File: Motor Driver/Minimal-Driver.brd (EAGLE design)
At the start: 49.6 x 13 mm, 9 parts, among them CN1 3p-2.54, Q1 CJ2302

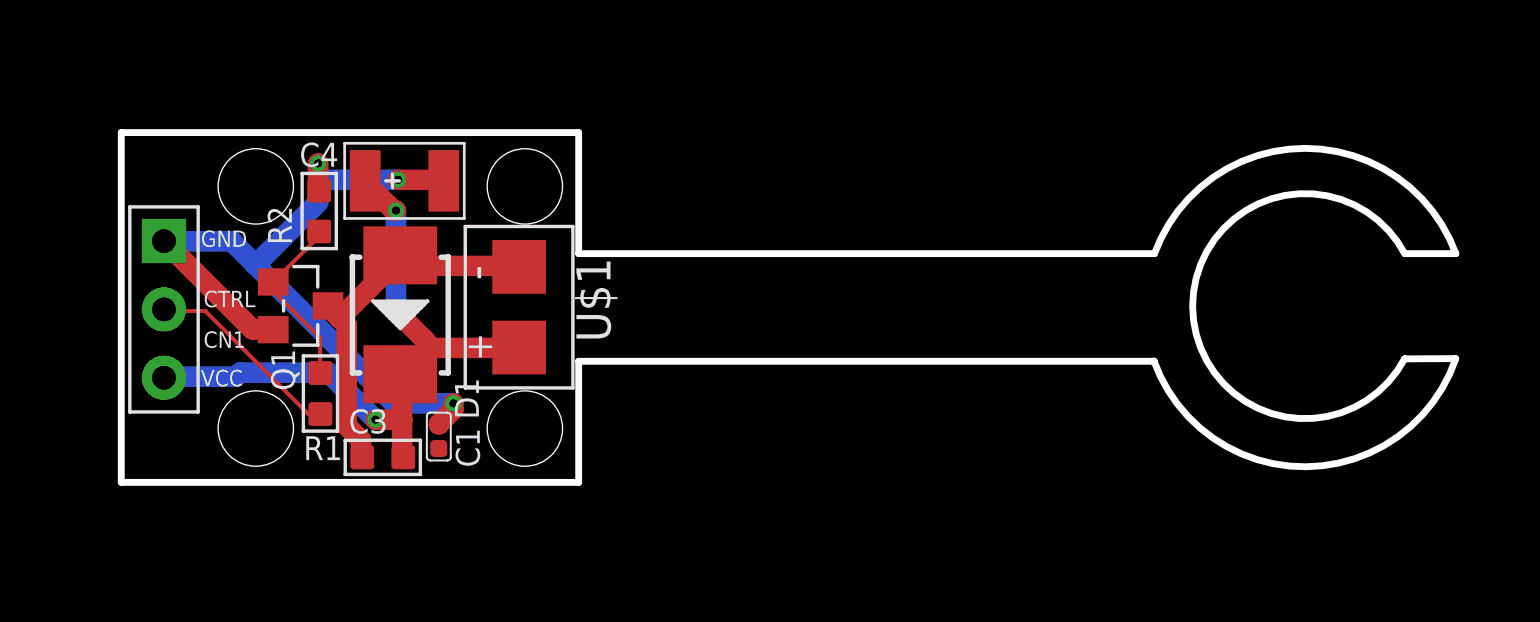
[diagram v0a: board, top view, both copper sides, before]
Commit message: New remote, new motor driver
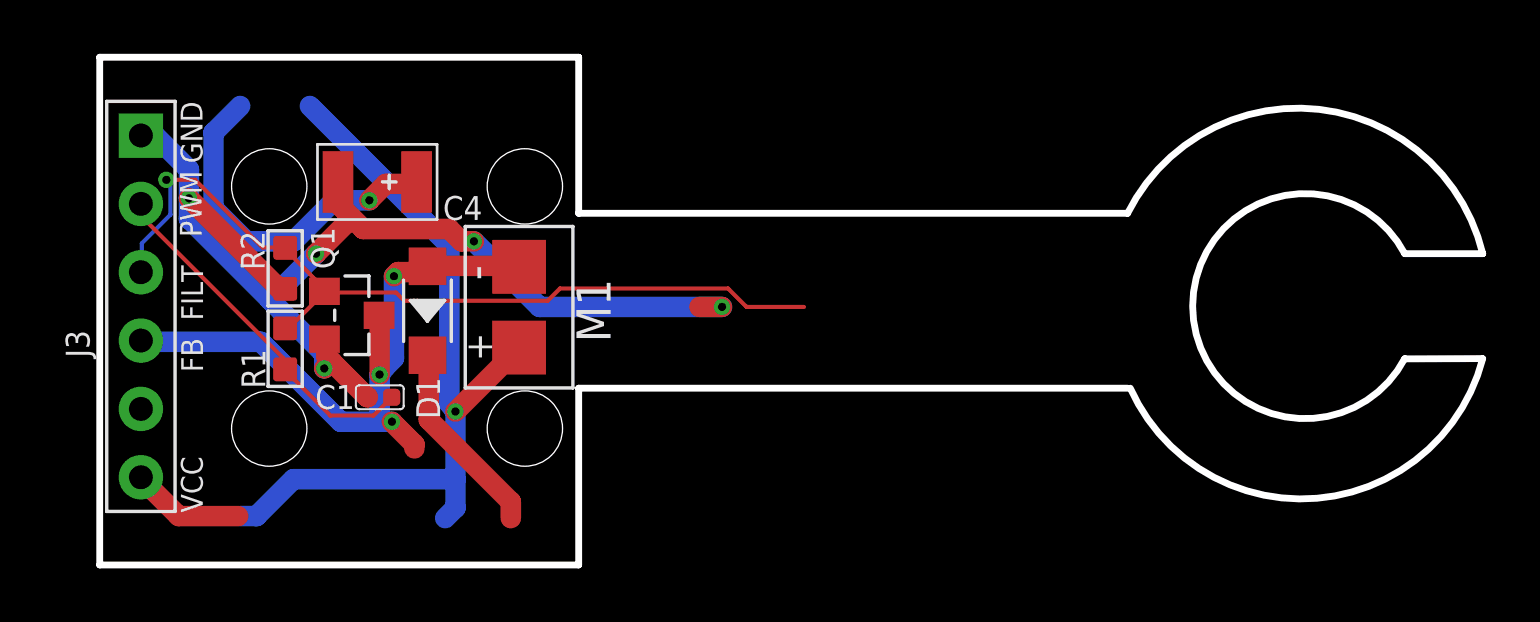
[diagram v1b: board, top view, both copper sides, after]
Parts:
- removed C3: 1uf, Seeed-Capacitor-2016:C0603
- removed CN1: 3p-2.54, Seeed-Connector -2016:H3-2.54
- added J3: 6p-2.54, Seeed-Connector -2016:H6-2.54
- D1: value 28V-5A -> 20V-500MA; device Seeed-Diode-2016:DO-214AA -> Seeed-Diode-2016:SOD-123
- moved C1 2.64 mm to (9.61, 2.66), turned to 90 degrees
- moved R2 2.48 mm to (6.09, 7.46), turned to 180 degrees
- moved R1 2.11 mm to (6.09, 4.46)
- moved Q1 1.93 mm to (8.57, 5.71)
- moved D1 1.02 mm to (11.4, 5.88)
- moved C4 1.01 mm to (9.52, 10.7), turned to 180 degrees
- renumbered U$1 to M1
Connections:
- removed net N$3: C1.2, CN1.2, R1.1
- removed net N$4: Q1.1, R1.2, R2.2
- removed net N$6: C3.1, D1.+, M1.V-, Q1.3
- new net FB: D1.+, J3.4, M1.V-, Q1.3
- new net FILT: J3.3, Q1.1, R1.2, R2.2
- new net PWM: C1.2, J3.2, R1.1
- net GND: now also J3.1; no longer CN1.1
- net VCC: now also J3.6; no longer C3.2, CN1.3
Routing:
- net FILT: track 0.00 -> 32.2 mm, vias 0 -> 1
- net VCC: track 24.9 -> 54.4 mm, vias 3 -> 2
- net FB: track 0.00 -> 24.6 mm, vias 0 -> 3
- net N$6: track 14.0 -> 0.00 mm
- net PWM: track 0.00 -> 13.4 mm
- net GND: track 30.2 -> 41.8 mm, vias 3 -> 5
- net N$3: track 7.45 -> 0.00 mm
- net N$4: track 6.71 -> 0.00 mm
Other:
- board size 49.6 x 13 mm -> 51.4 x 18.9 mm
- board text added: "FB"
- board text added: "FILT"
- board text added: "PWM"
- board text removed: "CTRL"

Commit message: cleanup
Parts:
- removed J3: 6p-2.54, Seeed-Connector -2016:H6-2.54
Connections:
- removed net FB: D1.+, J3.4, M1.V-, Q1.3
- removed net FILT: J3.3, Q1.1, R1.2, R2.2
- new net FILTERED: Q1.1, R1.2, R2.2
- new net FLYBACK: D1.+, M1.V-, Q1.3
- net GND: no longer J3.1
- net PWM: no longer J3.2
- net VCC: no longer J3.6
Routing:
- net FILT: track 32.2 -> 0.00 mm, vias 1 -> 0
- net FILTERED: track 0.00 -> 32.2 mm, vias 0 -> 1
- net FB: track 24.6 -> 0.00 mm, vias 3 -> 0
- net FLYBACK: track 0.00 -> 24.5 mm, vias 0 -> 3
- net VCC: track 54.4 -> 50.2 mm
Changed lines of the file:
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@@
 <attribute name="NAME" x="18.185" y="4.71" size="1.27" layer="21" rot="R90"/>
-</element>
-<element name="J3" library="Seeed-Connector -2016" package="H6-2.54" value="6p-2.54" x="0.73" y="6.04">
-<attribute name="MPN" value="P125-1106A1BS116A1" x="0.73" y="6.04" size="1.778" layer="27" display="off"/>
 </element>
 </elements>
@@
 <signal name="GND" class="1">
 <contactref element="C4" pad="-"/>
-<contactref element="Q1" pad="2"/>
-<contactref element="R2" pad="1"/>
-<contactref element="C1" pad="1"/>
-<contactref element="J3" pad="1"/>
 <wire x1="22.3266" y1="6.0198" x2="21.4884" y2="6.0198" width="0.762" layer="1"/>
 <wire x1="15.5448" y1="6.0198" x2="22.3266" y2="6.0198" width="0.762" layer="16"/>
@@
 <wire x1="7.8105" y1="4.0005" x2="9.144" y2="2.667" width="0.762" layer="1"/>
 <wire x1="7.62" y1="4.8006" x2="7.62" y2="4.191" width="0.762" layer="1"/>
-<wire x1="9.144" y1="2.667" x2="9.163" y2="2.6625" width="0.762" layer="1"/>
-<wire x1="7.62" y1="4.8006" x2="7.5515" y2="4.821" width="0.762" layer="1"/>
 <wire x1="5.8674" y1="6.7056" x2="6.0198" y2="6.7056" width="0.762" layer="1"/>
 <wire x1="2.5146" y1="10.0584" x2="5.8674" y2="6.7056" width="0.762" layer="1"/>
@@
 <wire x1="1.2954" y1="12.3444" x2="2.5146" y2="11.1252" width="0.762" layer="16"/>
 <wire x1="0.762" y1="12.3444" x2="1.2954" y2="12.3444" width="0.762" layer="16"/>
-<wire x1="6.0198" y1="6.7056" x2="6.0925" y2="6.693" width="0.762" layer="1"/>
-<wire x1="0.762" y1="12.3444" x2="0.73" y2="12.39" width="0.762" layer="16"/>
 <wire x1="7.5438" y1="4.2672" x2="7.5438" y2="3.7338" width="0.762" layer="16"/>
 <wire x1="2.5146" y1="9.2964" x2="5.5245" y2="6.2865" width="0.762" layer="16"/>
@@
 <via x="7.5438" y="3.7338" extent="1-16" drill="0.3048"/>
 <via x="7.239" y="8.001" extent="1-16" drill="0.3048"/>
+<contactref element="Q1" pad="2"/>
+<contactref element="R2" pad="1"/>
+<contactref element="C1" pad="1"/>
+<wire x1="6.0198" y1="6.7056" x2="6.0925" y2="6.693" width="0" layer="19" extent="1-1"/>
+<wire x1="9.163" y1="2.6625" x2="9.144" y2="2.667" width="0" layer="19" extent="1-1"/>
+<wire x1="7.5515" y1="4.821" x2="7.62" y2="4.8006" width="0" layer="19" extent="1-1"/>
 </signal>
 <signal name="VCC" class="1">
 <contactref element="M1" pad="V+"/>
-<contactref element="J3" pad="6"/>
-<wire x1="2.1336" y1="-1.7526" x2="4.3434" y2="-1.7526" width="0.762" layer="1"/>
-<wire x1="0.762" y1="-0.381" x2="2.1336" y2="-1.7526" width="0.762" layer="1"/>
-<wire x1="0.762" y1="-0.381" x2="0.73" y2="-0.31" width="0.762" layer="1"/>
 <wire x1="12.4206" y1="2.1336" x2="14.7828" y2="4.4958" width="0.762" layer="1"/>
 <wire x1="12.4206" y1="-1.4478" x2="12.4206" y2="-0.381" width="0.762" layer="16"/>
@@
 <wire x1="11.43" y1="4.191" x2="11.38" y2="4.2265" width="0.762" layer="1"/>
 <wire x1="12.192" y1="8.3058" x2="10.9728" y2="10.5918" width="0" layer="19" extent="1-16"/>
-<wire x1="4.3434" y1="-1.7526" x2="4.4196" y2="-1.7526" width="0" layer="19" extent="1-16"/>
 <wire x1="11.43" y1="1.8288" x2="12.192" y2="2.4384" width="0" layer="19" extent="1-16"/>
 </signal>
@@
 <contactref element="R1" pad="1"/>
 <contactref element="C1" pad="2"/>
-<contactref element="J3" pad="2"/>
 <wire x1="9.3726" y1="1.9812" x2="9.9822" y2="2.5908" width="0.1524" layer="1"/>
 <wire x1="7.7724" y1="1.9812" x2="9.3726" y2="1.9812" width="0.1524" layer="1"/>
@@
 <wire x1="0.762" y1="9.8298" x2="0.762" y2="9.3726" width="0.1524" layer="1"/>
 <wire x1="6.0198" y1="3.7338" x2="6.0925" y2="3.7005" width="0.1524" layer="1"/>
-<wire x1="0.762" y1="9.8298" x2="0.73" y2="9.85" width="0.1524" layer="1"/>
 </signal>
-<signal name="FILT">
+<signal name="FILTERED">
 <contactref element="R1" pad="2"/>
 <contactref element="R2" pad="2"/>
 <contactref element="Q1" pad="1"/>
-<contactref element="J3" pad="3"/>
 <wire x1="23.241" y1="6.0198" x2="25.3746" y2="6.0198" width="0.1524" layer="1"/>
 <wire x1="22.5552" y1="6.7056" x2="23.241" y2="6.0198" width="0.1524" layer="1"/>
@@
 <wire x1="5.2578" y1="8.2296" x2="2.7432" y2="10.7442" width="0.1524" layer="1"/>
 <wire x1="6.0198" y1="8.2296" x2="5.2578" y2="8.2296" width="0.1524" layer="1"/>
-<wire x1="0.762" y1="7.3152" x2="0.73" y2="7.31" width="0.1524" layer="16"/>
 <wire x1="6.0198" y1="8.2296" x2="6.0925" y2="8.217" width="0.1524" layer="1"/>
 <via x="1.6764" y="10.7442" extent="1-16" drill="0.3048"/>
 </signal>
-<signal name="FB" class="1">
+<signal name="FLYBACK" class="1">
 <contactref element="D1" pad="+"/>
 <contactref element="M1" pad="V-"/>
 <contactref element="Q1" pad="3"/>
-<contactref element="J3" pad="4"/>
 <wire x1="14.7828" y1="7.5438" x2="11.43" y2="7.5438" width="0.762" layer="1"/>
 <wire x1="11.43" y1="7.5438" x2="11.38" y2="7.5285" width="0.762" layer="1"/>
@@
 <wire x1="5.1816" y1="4.7244" x2="8.1534" y2="1.7526" width="0.762" layer="16"/>
 <wire x1="0.762" y1="4.7244" x2="5.1816" y2="4.7244" width="0.762" layer="16"/>
-<wire x1="0.762" y1="4.7244" x2="0.73" y2="4.77" width="0.762" layer="16"/>
 <wire x1="9.6012" y1="3.5052" x2="9.6012" y2="5.6388" width="0.762" layer="1"/>
 <wire x1="9.6012" y1="1.7526" x2="9.6012" y2="3.5052" width="0.762" layer="16"/>
